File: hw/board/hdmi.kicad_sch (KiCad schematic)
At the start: 3 parts, among them J1 HDMI_A, J2 HDMI_A, J3 Connector

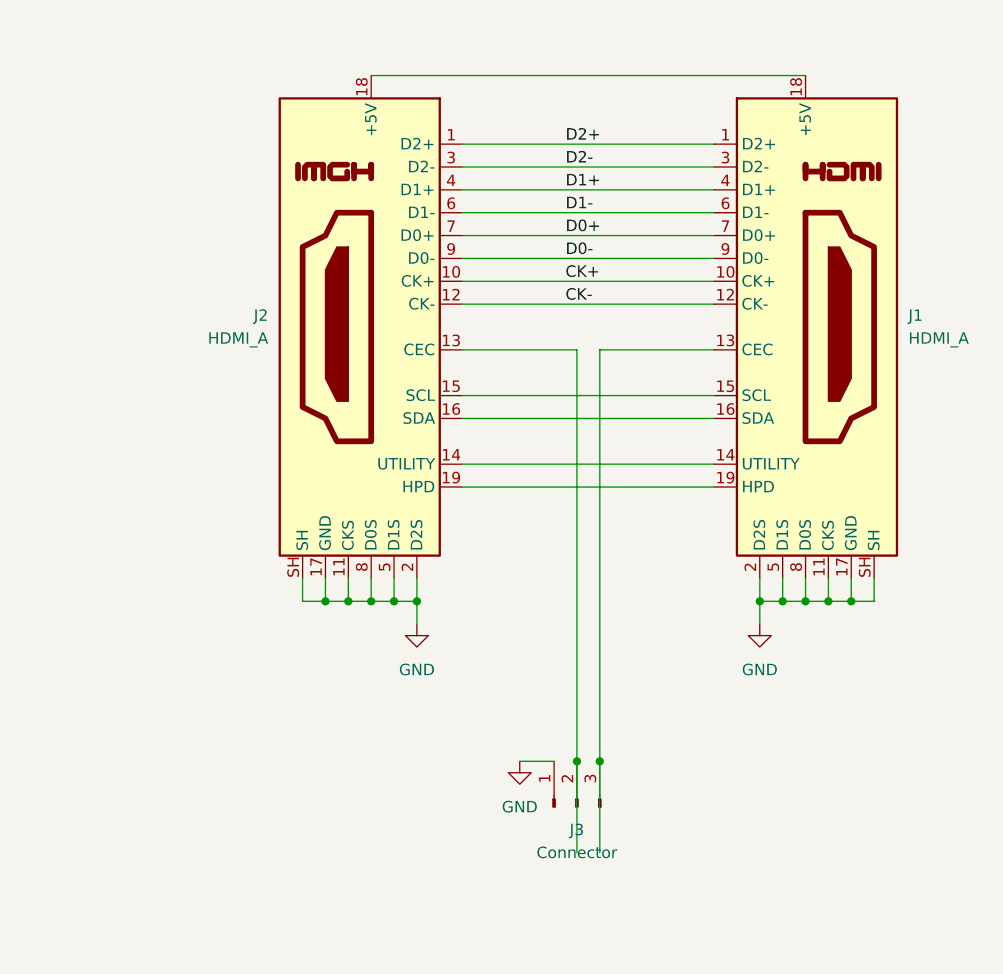
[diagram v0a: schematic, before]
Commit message: PCB with pullup resistors
Added 3.3v pin from Rpi to board, 27K Ohm pullup resistors, and diodes to conform to CEC spec.
Add cec-gpio configuration script.
Add HW specific readme.
Design is still just a guess.
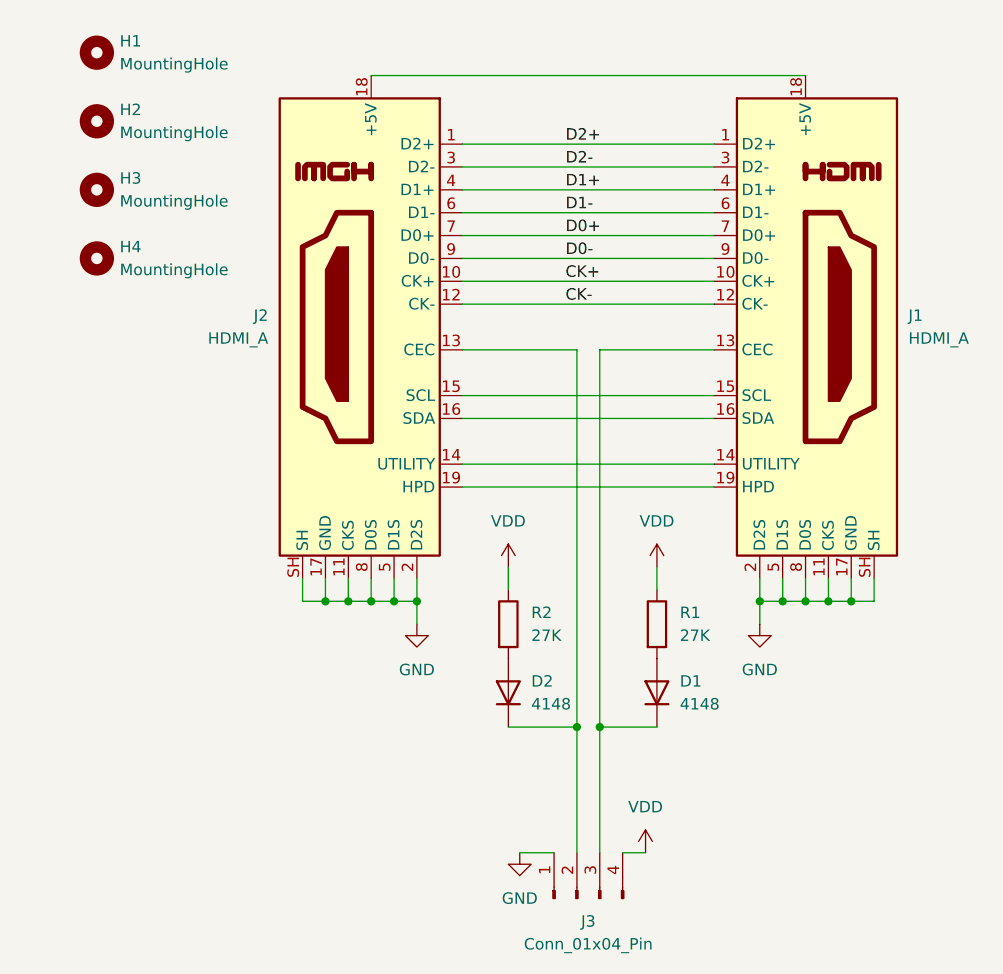
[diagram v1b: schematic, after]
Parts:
- removed J3: Connector, Connector_PinHeader_2.54mm:PinHeader_1x03_P2.54mm_Vertical, symbol Connector:Conn_01x03_Pin
- added D1, D2: 4148, Diode_SMD:D_0603_1608Metric, symbol Device:D
- added H1, H2, H3, H4: MountingHole, MountingHole:MountingHole_2.5mm, symbol Mechanical:MountingHole
- added J3: Conn_01x04_Pin, Connector_PinHeader_2.54mm:PinHeader_1x04_P2.54mm_Vertical, symbol Connector:Conn_01x04_Pin
- added R1, R2: 27K, Resistor_SMD:R_0603_1608Metric, symbol Device:R
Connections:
- net GND: now also J3.1 (Pin_1)
- net at J2.13 (CEC): now also D2.1 (K), J3.2 (Pin_2)
- net at J1.13 (CEC): now also D1.1 (K), J3.3 (Pin_3)
- new net: D1.2 (A), R1.2
- new net: D2.2 (A), R2.2
- new net VDD: J3.4 (Pin_4), R1.1, R2.1

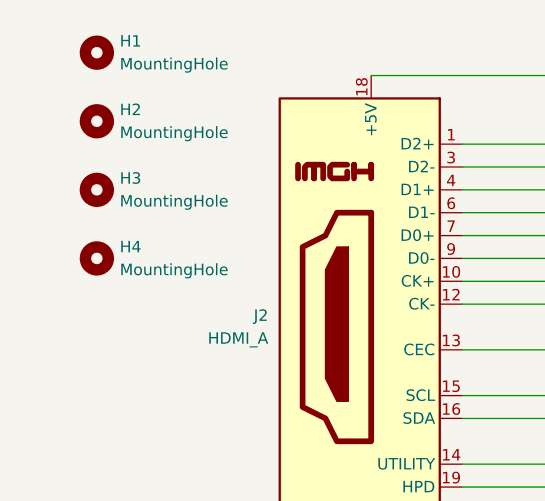
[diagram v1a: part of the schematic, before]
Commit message: PCB v2
4 Layers. More regular board dimensions. Thicker, straighter, shorter, better separated, equal length,
high speed traces.

No DRC violations.
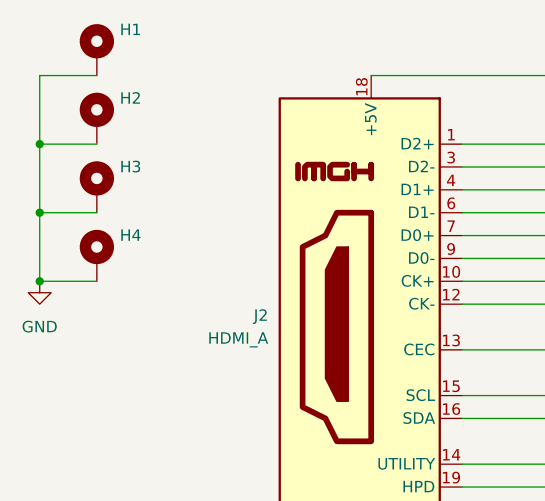
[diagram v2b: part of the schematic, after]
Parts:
- H1, H2, H3, H4: value MountingHole -> ~; footprint MountingHole:MountingHole_2.5mm -> MountingHole:MountingHole_2.5mm_Pad; symbol Mechanical:MountingHole -> Mechanical:MountingHole_Pad
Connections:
- net GND: now also H1.1, H2.1, H3.1, H4.1
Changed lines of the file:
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@@
 	(paper "A4")
+	(junction
+		(at 88.9 60.96)
+		(diameter 0)
+		(color 0 0 0 0)
+	)
 	(junction
 		(at 125.73 104.14)
@@
 	)
 	(junction
+		(at 88.9 53.34)
+		(diameter 0)
+		(color 0 0 0 0)
+	)
+	(junction
 		(at 176.53 104.14)
+		(diameter 0)
+		(color 0 0 0 0)
+	)
+	(junction
+		(at 88.9 68.58)
 		(diameter 0)
 		(color 0 0 0 0)
@@
 	(wire
 		(pts
+			(xy 88.9 45.72) (xy 88.9 53.34)
+		)
+		(stroke
+			(width 0)
+			(type default)
+		)
+	)
+	(wire
+		(pts
 			(xy 176.53 101.6) (xy 176.53 104.14)
 		)
@@
 	(wire
 		(pts
+			(xy 95.25 60.96) (xy 88.9 60.96)
+		)
+		(stroke
+			(width 0)
+			(type default)
+		)
+	)
+	(wire
+		(pts
 			(xy 168.91 101.6) (xy 168.91 104.14)
 		)
@@
 	(wire
 		(pts
+			(xy 88.9 60.96) (xy 88.9 68.58)
+		)
+		(stroke
+			(width 0)
+			(type default)
+		)
+	)
+	(wire
+		(pts
 			(xy 135.89 68.58) (xy 163.83 68.58)
 		)
@@
 	(wire
 		(pts
+			(xy 95.25 45.72) (xy 88.9 45.72)
+		)
+		(stroke
+			(width 0)
+			(type default)
+		)
+	)
+	(wire
+		(pts
 			(xy 123.19 101.6) (xy 123.19 104.14)
 		)
@@
 	(wire
 		(pts
+			(xy 88.9 53.34) (xy 88.9 60.96)
+		)
+		(stroke
+			(width 0)
+			(type default)
+		)
+	)
+	(wire
+		(pts
 			(xy 179.07 104.14) (xy 181.61 104.14)
 		)
@@
 	(wire
 		(pts
+			(xy 95.25 53.34) (xy 88.9 53.34)
+		)
+		(stroke
+			(width 0)
+			(type default)
+		)
+	)
+	(wire
+		(pts
 			(xy 128.27 101.6) (xy 128.27 104.14)
 		)
@@
 		(pts
 			(xy 125.73 101.6) (xy 125.73 104.14)
+		)
+		(stroke
+			(width 0)
+			(type default)
+		)
+	)
+	(wire
+		(pts
+			(xy 88.9 68.58) (xy 95.25 68.58)
 		)
 		(stroke
@@
 			)
 		)
-		(property "Datasheet" "https://www.digikey.com/en/products/detail/bourns-inc/CR0603-JW-273ELF/3784345"
+		(property "Datasheet" "https://www.digikey.com/en/products/detail/würth-elektronik/61300411121/4846827"
 			(at 148.59 137.16 0)
 			(effects
@@
 			)
 		)
-		(property "Datasheet" "https://www.digikey.com/en/products/detail/bourns-inc/CR0603-JW-273ELF/3784345"
+		(property "Datasheet" "https://www.digikey.com/en/products/detail/taiwan-semiconductor-corporation/TS4148-RCG/7359811"
 			(at 157.48 114.3 0)
 			(effects
@@
 	)
 	(symbol
-		(lib_id "Mechanical:MountingHole")
+		(lib_id "power:GND")
+		(at 88.9 68.58 0)
+		(unit 1)
+		(exclude_from_sim no)
+		(in_bom yes)
+		(on_board yes)
+		(dnp no)
+		(fields_autoplaced yes)
+		(property "Reference" "#PWR07"
+			(at 88.9 74.93 0)
+			(effects
+				(font
+					(size 1.27 1.27)
+				)
+				(hide yes)
+			)
+		)
+		(property "Value" "GND"
+			(at 88.9 73.66 0)
+			(effects
+				(font
+					(size 1.27 1.27)
+				)
+			)
+		)
+		(property "Footprint" ""
+			(at 88.9 68.58 0)
+			(effects
+				(font
+					(size 1.27 1.27)
+				)
+				(hide yes)
+			)
+		)
+		(property "Datasheet" ""
+			(at 88.9 68.58 0)
+			(effects
+				(font
+					(size 1.27 1.27)
+				)
+				(hide yes)
+			)
+		)
+		(property "Description" "Power symbol creates a global label with name \"GND\" , ground"
+			(at 88.9 68.58 0)
+			(effects
+				(font
+					(size 1.27 1.27)
+				)
+				(hide yes)
+			)
+		)
+		(pin "1"
+		)
+		(instances
+			(project ""
+				(path "/d9471c7f-fc59-4490-a852-252dc0a6feaf"
+					(reference "#PWR07")
+					(unit 1)
+				)
+			)
+		)
+	)
+	(symbol
+		(lib_id "Mechanical:MountingHole_Pad")
 		(at 95.25 58.42 0)
 		(unit 1)
@@
 		(fields_autoplaced yes)
 		(property "Reference" "H3"
-			(at 97.79 57.1499 0)
+			(at 97.79 55.8799 0)
 			(effects
 				(font
@@
 			)
 		)
-		(property "Value" "MountingHole"
-			(at 97.79 59.6899 0)
+		(property "Value" "~"
+			(at 97.79 58.4199 0)
 			(effects
 				(font
@@
 			)
 		)
-		(property "Footprint" "MountingHole:MountingHole_2.5mm"
+		(property "Footprint" "MountingHole:MountingHole_2.5mm_Pad"
 			(at 95.25 58.42 0)
 			(effects
@@
 			)
 		)
-		(property "Description" "Mounting Hole without connection"
+		(property "Description" "Mounting Hole with connection"
 			(at 95.25 58.42 0)
 			(effects
@@
 				(hide yes)
 			)
+		)
+		(pin "1"
 		)
 		(instances
@@
 	)
 	(symbol
-		(lib_id "Mechanical:MountingHole")
+		(lib_id "Mechanical:MountingHole_Pad")
 		(at 95.25 43.18 0)
 		(unit 1)
@@
 		(fields_autoplaced yes)
 		(property "Reference" "H1"
-			(at 97.79 41.9099 0)
+			(at 97.79 40.6399 0)
 			(effects
 				(font
@@
 			)
 		)
-		(property "Value" "MountingHole"
-			(at 97.79 44.4499 0)
+		(property "Value" "~"
+			(at 97.79 43.1799 0)
 			(effects
 				(font
@@
 			)
 		)
-		(property "Footprint" "MountingHole:MountingHole_2.5mm"
+		(property "Footprint" "MountingHole:MountingHole_2.5mm_Pad"
 			(at 95.25 43.18 0)
 			(effects
@@
 			)
 		)
-		(property "Description" "Mounting Hole without connection"
+		(property "Description" "Mounting Hole with connection"
 			(at 95.25 43.18 0)
 			(effects
@@
 				(hide yes)
 			)
+		)
+		(pin "1"
 		)
 		(instances
@@
 	)
 	(symbol
-		(lib_id "Mechanical:MountingHole")
+		(lib_id "Mechanical:MountingHole_Pad")
 		(at 95.25 66.04 0)
 		(unit 1)
@@
 		(fields_autoplaced yes)
 		(property "Reference" "H4"
-			(at 97.79 64.7699 0)
+			(at 97.79 63.4999 0)
 			(effects
 				(font
@@
 			)
 		)
-		(property "Value" "MountingHole"
-			(at 97.79 67.3099 0)
+		(property "Value" "~"
+			(at 97.79 66.0399 0)
 			(effects
 				(font
@@
 			)
 		)
-		(property "Footprint" "MountingHole:MountingHole_2.5mm"
+		(property "Footprint" "MountingHole:MountingHole_2.5mm_Pad"
 			(at 95.25 66.04 0)
 			(effects
@@
 			)
 		)
-		(property "Description" "Mounting Hole without connection"
+		(property "Description" "Mounting Hole with connection"
 			(at 95.25 66.04 0)
 			(effects
@@
 				(hide yes)
 			)
+		)
+		(pin "1"
 		)
 		(instances
@@
 			)
 		)
-		(property "Datasheet" "https://www.digikey.com/en/products/detail/bourns-inc/CR0603-JW-273ELF/3784345"
+		(property "Datasheet" "https://www.digikey.com/en/products/detail/taiwan-semiconductor-corporation/TS4148-RCG/7359811"
 			(at 140.97 114.3 0)
 			(effects
@@
 	)
 	(symbol
-		(lib_id "Mechanical:MountingHole")
+		(lib_id "Mechanical:MountingHole_Pad")
 		(at 95.25 50.8 0)
 		(unit 1)
@@
 		(fields_autoplaced yes)
 		(property "Reference" "H2"
-			(at 97.79 49.5299 0)
+			(at 97.79 48.2599 0)
 			(effects
 				(font
@@
 			)
 		)
-		(property "Value" "MountingHole"
-			(at 97.79 52.0699 0)
+		(property "Value" "~"
+			(at 97.79 50.7999 0)
 			(effects
 				(font
@@
 			)
 		)
-		(property "Footprint" "MountingHole:MountingHole_2.5mm"
+		(property "Footprint" "MountingHole:MountingHole_2.5mm_Pad"
 			(at 95.25 50.8 0)
 			(effects
@@
 			)
 		)
-		(property "Description" "Mounting Hole without connection"
+		(property "Description" "Mounting Hole with connection"
 			(at 95.25 50.8 0)
 			(effects
@@
 			)
 		)
+		(pin "1"
+		)
 		(instances
